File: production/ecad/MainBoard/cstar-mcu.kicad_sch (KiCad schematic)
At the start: 68 parts, among them J25 TYPE-C-31-M-12, J3 RX connect, J31 TYPE-C-31-M-12, J4 TX connect, J5 Ultra_1, J6 Ultra_2, J7 Ultra_3, J8 Ultra_4, Q1 AO3400A, Q2 AO3400A, Q3 AO3400A, Q4 AO3400A, SW1 SW_Push, SW2 SW_Push, SW3 SW_Push, SW4 SW_Push, U1 ESP32-WROOM-32UE_M113EH6400UH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, U10 TCA9534PWR, U2 CP2102N-A01-GQFN28, U3 TXB0104DR, U4 CP2102N-A01-GQFN28, U5 TXB0104DR, U6 ESP32-WROOM-32UE_M113EH6400UH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

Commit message: fixed some sch mistakes, more layout
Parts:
- removed R9 (x2): 4.7k, Resistor_SMD:R_0805_2012Metric, symbol Device:R
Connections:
- net +3.3V is gone; now on net +3V3: R9.2, R9.2, R9.2, R9.2, R9.2, U10.16 (VCC), U3.1 (VCCA), U5.1 (VCCA)

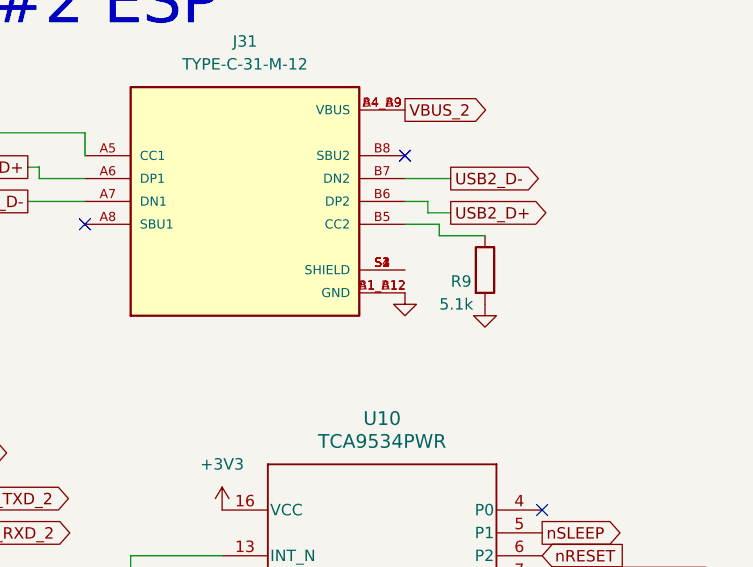
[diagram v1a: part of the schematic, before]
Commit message: ALL DRC ERRORS FIXED
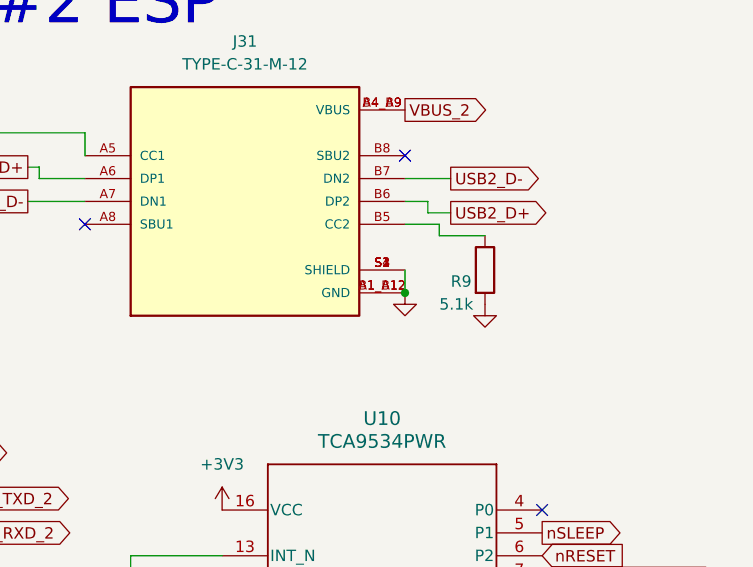
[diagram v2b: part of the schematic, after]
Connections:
- net GND: now also J31.S1 (SHIELD), J31.S2 (SHIELD), J31.S3 (SHIELD), J31.S4 (SHIELD)
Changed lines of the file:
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@@
   (junction (at 36.83 148.59) (diameter 0) (color 0 0 0 0)
+  )
+  (junction (at 377.19 137.16) (diameter 0) (color 0 0 0 0)
   )
   (junction (at 177.165 24.765) (diameter 0) (color 0 0 0 0)
@@
     (stroke (width 0) (type default))
   )
+  (wire (pts (xy 377.19 134.62) (xy 377.19 137.16))
+    (stroke (width 0) (type default))
+  )

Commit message: fixed usbc
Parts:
- removed J25, J31: TYPE-C-31-M-12, CSTAR-MainBoard-Footprints:HRO_TYPE-C-31-M-12, symbol TYPE-C-31-M-12:TYPE-C-31-M-12
- removed R9 (x4): 5.1k, Resistor_SMD:R_0805_2012Metric, symbol Device:R
- added J25, J27: DX07S016JA3R1500, CONN12_DX07S_JAE, symbol usbc:DX07S016JA3R1500
- added R9 (x4): 5.1k, Resistor_SMD:R_0805_2012Metric, symbol Device:R
- added R9 (x2): 4.7k, Resistor_SMD:R_0805_2012Metric, symbol Device:R
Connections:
- net USB1_D- is gone; now on net USB1_D+: U2.5 (D-)
- net USB2_D- is gone; now on net USB2_D+: U4.5 (D-)
- net +3V3: now also R9.1, R9.1; no longer R9.2, R9.2, R9.2, R9.2, R9.2, U10.16 (VCC), U3.1 (VCCA), U5.1 (VCCA)
- net GND: now also J25.1 (GND), J25.12 (GND), J27.1 (GND), J27.12 (GND), R9.2, R9.2, R9.2, R9.2
- net SCL: now also R9.2
- net SDA: now also R9.2
- net USB1_D+: now also J27.5 (D-), J27.6 (D+), J27.7 (D+), J27.8 (D-)
- net USB2_D+: now also J25.5 (D-), J25.6 (D+), J25.7 (D+)
- net VBUS_1: now also J27.11 (VBUS), J27.2 (VBUS)
- net VBUS_2: now also J25.11 (VBUS), J25.2 (VBUS)
- new net: J25.3 (CC1), R9.1
- new net: J27.3 (CC1), R9.1
- new net: J25.9 (CC2), R9.1
- new net: J27.9 (CC2), R9.1
- new net +3.3V: R9.2, R9.2, R9.2, R9.2, R9.2, U10.16 (VCC), U3.1 (VCCA), U5.1 (VCCA)

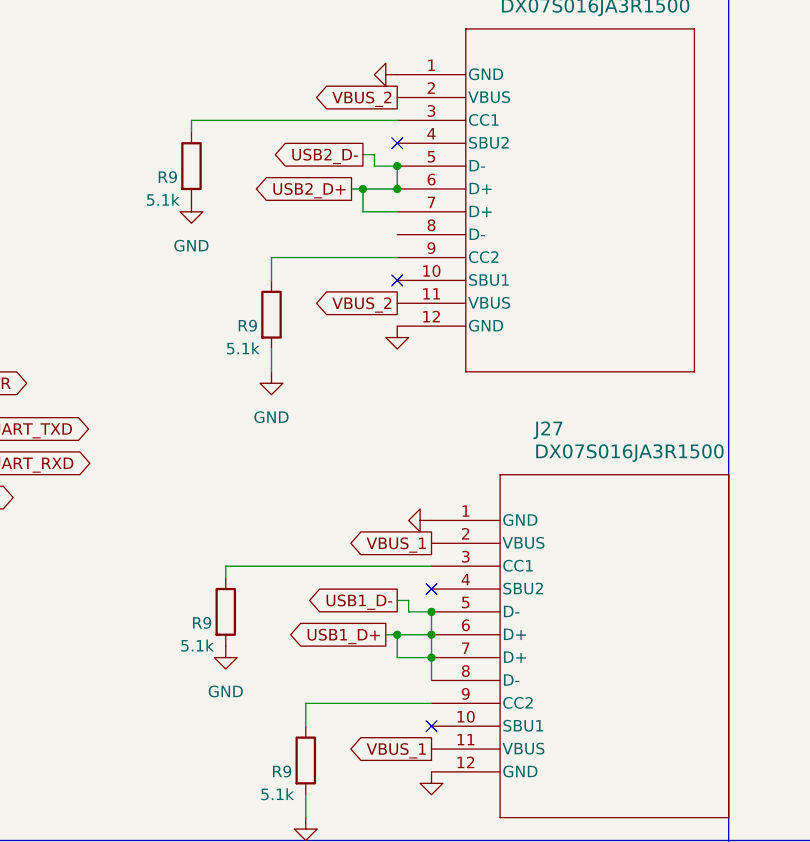
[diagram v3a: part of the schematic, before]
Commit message: fixed cats weird usbc thing (FIX YOUR FOOTPRINT)
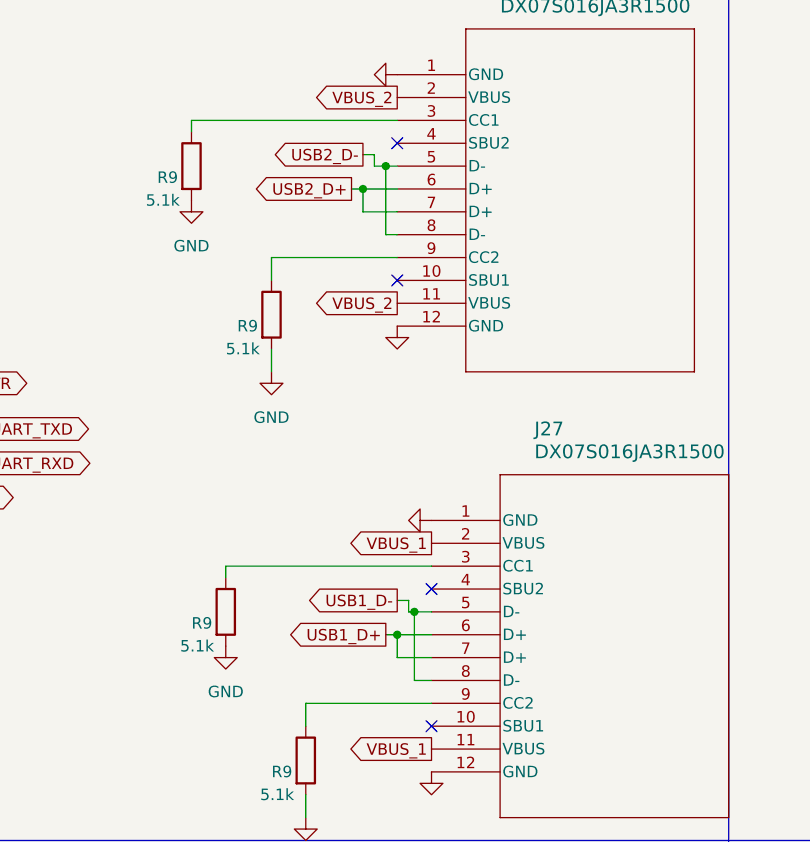
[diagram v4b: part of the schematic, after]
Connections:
- net USB1_D+: no longer J27.5 (D-), J27.8 (D-), U2.5 (D-)
- net USB2_D+: no longer J25.5 (D-), U4.5 (D-)
- net USB2_D-: now reaches J25.8 (D-)
- net USB2_D-: now also J25.5 (D-), U4.5 (D-)
- new net USB1_D-: J27.5 (D-), J27.8 (D-), U2.5 (D-)
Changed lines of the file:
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@@
   (junction (at 383.54 23.495) (diameter 0) (color 0 0 0 0)
   )
+  (junction (at 171.45 128.27) (diameter 0) (color 0 0 0 0)
+  )
   (junction (at 322.58 224.79) (diameter 0) (color 0 0 0 0)
   )
@@
   (junction (at 196.85 34.925) (diameter 0) (color 0 0 0 0)
   )
-  (junction (at 172.72 130.81) (diameter 0) (color 0 0 0 0)
-  )
   (junction (at 168.91 130.81) (diameter 0) (color 0 0 0 0)
   )
@@
   (junction (at 245.11 167.64) (diameter 0) (color 0 0 0 0)
   )
-  (junction (at 176.53 177.8) (diameter 0) (color 0 0 0 0)
-  )
   (junction (at 392.43 222.25) (diameter 0) (color 0 0 0 0)
   )
@@
   (junction (at 398.78 55.88) (diameter 0) (color 0 0 0 0)
   )
-  (junction (at 176.53 182.88) (diameter 0) (color 0 0 0 0)
-  )
   (junction (at 133.35 251.46) (diameter 0) (color 0 0 0 0)
   )
@@
   (junction (at 356.87 186.69) (diameter 0) (color 0 0 0 0)
   )
-  (junction (at 176.53 180.34) (diameter 0) (color 0 0 0 0)
-  )
   (junction (at 387.35 33.655) (diameter 0) (color 0 0 0 0)
   )
   (junction (at 193.675 24.765) (diameter 0) (color 0 0 0 0)
   )
-  (junction (at 172.72 128.27) (diameter 0) (color 0 0 0 0)
+  (junction (at 174.625 177.8) (diameter 0) (color 0 0 0 0)
   )
   (junction (at 36.83 139.7) (diameter 0) (color 0 0 0 0)
@@
     (stroke (width 0) (type default))
   )
+  (wire (pts (xy 172.72 182.88) (xy 176.53 182.88))
+    (stroke (width 0) (type default))
+  )
   (wire (pts (xy 383.54 23.495) (xy 383.54 26.035))
     (stroke (width 0) (type default))
@@
   )
   (wire (pts (xy 248.92 167.64) (xy 245.11 167.64))
+    (stroke (width 0) (type default))
+  )
+  (wire (pts (xy 171.45 128.27) (xy 170.18 128.27))
     (stroke (width 0) (type default))
   )
@@
     (stroke (width 0) (type default))
   )
-  (wire (pts (xy 176.53 177.8) (xy 173.99 177.8))
+  (wire (pts (xy 174.625 177.8) (xy 173.99 177.8))
+    (stroke (width 0) (type default))
+  )
+  (wire (pts (xy 176.53 177.8) (xy 174.625 177.8))
     (stroke (width 0) (type default))
   )
@@
     (stroke (width 0) (type default))
   )
-  (wire (pts (xy 172.72 128.27) (xy 170.18 128.27))
+  (wire (pts (xy 172.72 128.27) (xy 171.45 128.27))
     (stroke (width 0) (type default))
   )
@@
   )
   (wire (pts (xy 346.71 181.61) (xy 346.71 185.42))
+    (stroke (width 0) (type default))
+  )
+  (wire (pts (xy 174.625 177.8) (xy 174.625 185.42))
     (stroke (width 0) (type default))
   )
@@
     (stroke (width 0) (type default))
   )
-  (wire (pts (xy 176.53 182.88) (xy 172.72 182.88))
-    (stroke (width 0) (type default))
-  )
   (wire (pts (xy 369.57 73.66) (xy 369.57 71.12))
     (stroke (width 0) (type default))
@@
     (stroke (width 0) (type default))
   )
-  (wire (pts (xy 176.53 180.34) (xy 176.53 182.88))
-    (stroke (width 0) (type default))
-  )
   (wire (pts (xy 115.57 162.56) (xy 119.38 162.56))
     (stroke (width 0) (type default))
@@
     (stroke (width 0) (type default))
   )
-  (wire (pts (xy 176.53 182.88) (xy 176.53 185.42))
-    (stroke (width 0) (type default))
-  )
   (wire (pts (xy 361.95 60.96) (xy 364.49 60.96))
     (stroke (width 0) (type default))
@@
     (stroke (width 0) (type default))
   )
+  (wire (pts (xy 171.45 128.27) (xy 171.45 135.89))
+    (stroke (width 0) (type default))
+  )
   (wire (pts (xy 361.95 45.72) (xy 368.3 45.72))
     (stroke (width 0) (type default))
@@
     (stroke (width 0) (type default))
   )
-  (wire (pts (xy 176.53 177.8) (xy 176.53 180.34))
-    (stroke (width 0) (type default))
-  )
   (wire (pts (xy 177.165 24.765) (xy 193.675 24.765))
     (stroke (width 0) (type default))
@@
   )
   (wire (pts (xy 401.32 48.26) (xy 398.78 48.26))
+    (stroke (width 0) (type default))
+  )
+  (wire (pts (xy 174.625 185.42) (xy 176.53 185.42))
     (stroke (width 0) (type default))
   )
@@
     (stroke (width 0) (type default))
   )
+  (wire (pts (xy 171.45 135.89) (xy 172.72 135.89))
+    (stroke (width 0) (type default))
+  )
   (wire (pts (xy 118.11 144.78) (xy 115.57 144.78))
     (stroke (width 0) (type default))
@@
     (stroke (width 0) (type default))
   )
-  (wire (pts (xy 172.72 128.27) (xy 172.72 130.81))
-    (stroke (width 0) (type default))
-  )

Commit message: fixed, please for the love of god Kaden dont find any mistakes
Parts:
- removed J25, J27: DX07S016JA3R1500, CONN12_DX07S_JAE, symbol usbc:DX07S016JA3R1500
- removed R9 (x4): 5.1k, Resistor_SMD:R_0805_2012Metric, symbol Device:R
- added J25, J31: USB4105-GF-A, USB4105_GCT, symbol usbfinal:USB4105-GF-A
- added R9 (x4): 5.1k, Resistor_SMD:R_0805_2012Metric, symbol Device:R
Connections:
- net GND: now also J25.A1-B12 (GND), J25.B1-A12 (GND), J31.A1-B12 (GND), J31.B1-A12 (GND), R9.2, R9.2, R9.2, R9.2
- net USB1_D+: now also J25.A6 (DP1), J25.B6 (DP2)
- net USB1_D-: now also J25.A7 (DN1), J25.B7 (DN2)
- net USB2_D+: now also J31.A6 (DP1), J31.B6 (DP2)
- net USB2_D-: now also J31.A7 (DN1), J31.B7 (DN2)
- net VBUS_1: now also J25.A4-B9 (VBUS), J25.B4-A9 (VBUS)
- net VBUS_2: now also J31.A4-B9 (VBUS), J31.B4-A9 (VBUS)
- new net: J25.B5 (CC2), R9.1
- new net: J31.A5 (CC1), R9.1
- new net: J31.B5 (CC2), R9.1
- new net: J25.A5 (CC1), R9.1

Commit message: i swear to god kaden this should work
I checked the footprint twice in foortprint editor and everything looks good. I checked to make sure its assigned
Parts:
- removed J25, J31: USB4105-GF-A, USB4105_GCT, symbol usbfinal:USB4105-GF-A
- removed R9 (x4): 5.1k, Resistor_SMD:R_0805_2012Metric, symbol Device:R
- added J27, J31: 1332645, 1332645:PHOENIX_1332645, symbol 1332645:1332645
- added R9 (x4): 5.1k, Resistor_SMD:R_0805_2012Metric, symbol Device:R
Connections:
- net GND: now also J27.A1_B12 (GND_A), J27.B1_A12 (GND_B), J27.SH1 (SHIELD), J27.SH2 (SHIELD__1), J27.SH3 (SHIELD__2), J27.SH4 (SHIELD__3), J31.A1_B12 (GND_A), J31.B1_A12 (GND_B), J31.SH1 (SHIELD), J31.SH2 (SHIELD__1), J31.SH3 (SHIELD__2), J31.SH4 (SHIELD__3), R9.2, R9.2, R9.2, R9.2
- net USB1_D+: now also J31.A6 (DP1), J31.B6 (DP2)
- net USB1_D-: now also J31.A7 (DN1), J31.B7 (DN2)
- net USB2_D+: now also J27.A6 (DP1), J27.B6 (DP2)
- net USB2_D-: now also J27.A7 (DN1), J27.B7 (DN2)
- net VBUS_1: now also J31.A4_B9 (VBUS_A), J31.B4_A9 (VBUS_B)
- net VBUS_2: now also J27.A4_B9 (VBUS_A), J27.B4_A9 (VBUS_B)
- new net: J31.A5 (CC1), R9.1
- new net: J27.B5 (CC2), R9.1
- new net: J31.B5 (CC2), R9.1
- new net: J27.A5 (CC1), R9.1

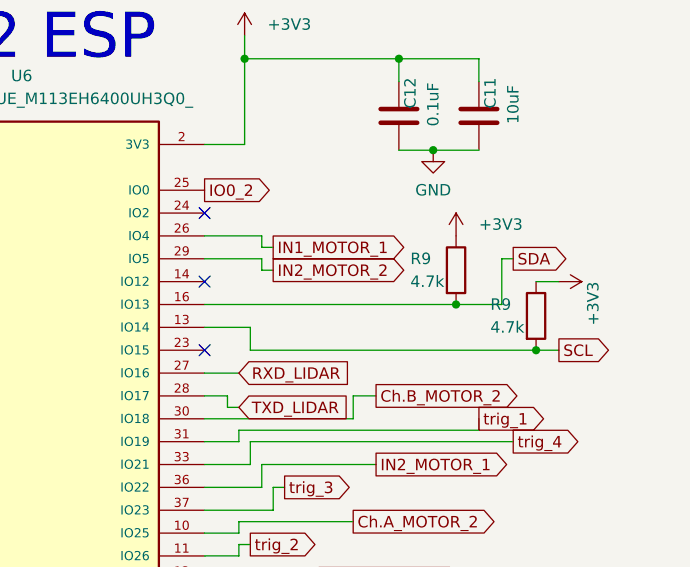
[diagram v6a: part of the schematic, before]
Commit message: updated with correct USBC -- still need to fix added DRCs
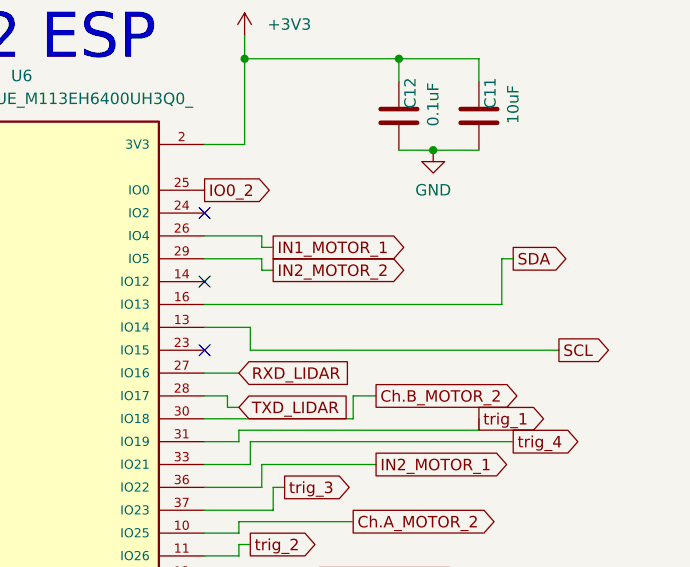
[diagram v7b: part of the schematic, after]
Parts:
- removed R9 (x2): 4.7k, Resistor_SMD:R_0805_2012Metric, symbol Device:R
- J27, J31: footprint 1332645:PHOENIX_1332645 -> CSTAR-MainBoard-Footprints:PHOENIX_1332645
- U10: footprint PW0016A-IPC_A -> CSTAR-MainBoard-Footprints:PW0016A-IPC_A
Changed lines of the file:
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@@
   (junction (at 392.43 222.25) (diameter 0) (color 0 0 0 0)
   )
-  (junction (at 389.89 50.8) (diameter 0) (color 0 0 0 0)
-  )
   (junction (at 236.22 151.13) (diameter 0) (color 0 0 0 0)
   )
@@
   (junction (at 45.72 165.1) (diameter 0) (color 0 0 0 0)
   )
-  (junction (at 398.78 55.88) (diameter 0) (color 0 0 0 0)
-  )
   (junction (at 157.48 138.43) (diameter 0) (color 0 0 0 0)
   )
@@
     (stroke (width 0) (type default))
   )
-  (wire (pts (xy 389.89 50.8) (xy 394.97 50.8))
+  (wire (pts (xy 361.95 50.8) (xy 394.97 50.8))
     (stroke (width 0) (type default))
   )
@@
     (stroke (width 0) (type default))
   )
-  (wire (pts (xy 389.89 50.8) (xy 361.95 50.8))
-    (stroke (width 0) (type default))
-  )
   (wire (pts (xy 264.16 231.14) (xy 264.16 224.79))
     (stroke (width 0) (type default))
@@
     (stroke (width 0) (type default))
   )
-  (wire (pts (xy 401.32 48.26) (xy 398.78 48.26))
-    (stroke (width 0) (type default))
-  )
   (wire (pts (xy 48.26 153.67) (xy 48.26 154.94))
     (stroke (width 0) (type default))
@@
     (stroke (width 0) (type default))
   )
-  (wire (pts (xy 398.78 55.88) (xy 401.32 55.88))
+  (wire (pts (xy 367.03 55.88) (xy 401.32 55.88))
     (stroke (width 0) (type default))
   )
@@
     (stroke (width 0) (type default))
   )
-  (wire (pts (xy 367.03 55.88) (xy 398.78 55.88))
-    (stroke (width 0) (type default))
-  )
   (wire (pts (xy 228.6 171.45) (xy 228.6 167.64))
     (stroke (width 0) (type default))
@@
       (effects (font (size 1.524 1.524)))
     )
-    (property "Footprint" "PW0016A-IPC_A" (at 356.87 161.29 0)
+    (property "Footprint" "CSTAR-MainBoard-Footprints:PW0016A-IPC_A" (at 356.87 161.29 0)
       (effects (font (size 1.27 1.27) italic) hide)
     )
@@
     )
   )
-  (symbol (lib_id "Device:R") (at 398.78 52.07 0) (unit 1)
-    (in_bom yes) (on_board yes) (dnp no)
-    (property "Reference" "R9" (at 393.7 50.8 0)
-      (effects (font (size 1.27 1.27)) (justify left))
-    )
-    (property "Value" "4.7k" (at 393.7 53.34 0)
-      (effects (font (size 1.27 1.27)) (justify left))
-    )
-    (property "Footprint" "Resistor_SMD:R_0805_2012Metric" (at 397.002 52.07 90)
-      (effects (font (size 1.27 1.27)) hide)
-    )
-    (property "Datasheet" "~" (at 398.78 52.07 0)
-      (effects (font (size 1.27 1.27)) hide)
-    )
-    (pin "1")
-    (pin "2")
-    (instances
-      (project "cstar-mcu"
-        (path "/889d461f-2713-421f-88e2-0d0ce2e66089"
-          (reference "R9") (unit 1)
-        )
-      )
-      (project "CSTAR"
-        (path "/cd9fa943-c6eb-468b-990c-ea873c442553/ab376fb8-b3cc-4961-835f-6ea621157706"
-          (reference "R56") (unit 1)
-        )
-      )
-    )
-  )
   (symbol (lib_id "power:GND") (at 22.86 25.4 270) (unit 1)
     (in_bom yes) (on_board yes) (dnp no) (fields_autoplaced)
@@
     )
   )
-  (symbol (lib_id "power:+3V3") (at 389.89 43.18 0) (unit 1)
-    (in_bom yes) (on_board yes) (dnp no)
-    (property "Reference" "#PWR057" (at 389.89 46.99 0)
-      (effects (font (size 1.27 1.27)) hide)
-    )
-    (property "Value" "+3V3" (at 392.43 41.91 0)
-      (effects (font (size 1.27 1.27)) (justify left))
-    )
-    (property "Footprint" "" (at 389.89 43.18 0)
-      (effects (font (size 1.27 1.27)) hide)
-    )
-    (property "Datasheet" "" (at 389.89 43.18 0)
-      (effects (font (size 1.27 1.27)) hide)
-    )
-    (pin "1")
-    (instances
-      (project "cstar-mcu"
-        (path "/889d461f-2713-421f-88e2-0d0ce2e66089"
-          (reference "#PWR057") (unit 1)
-        )
-      )
-      (project "CSTAR"
-        (path "/cd9fa943-c6eb-468b-990c-ea873c442553/ab376fb8-b3cc-4961-835f-6ea621157706"
-          (reference "#PWR0141") (unit 1)
-        )
-      )
-    )
-  )
   (symbol (lib_id "ESP32-WROOM-32UE_M113EH6400UH3Q0_:ESP32-WROOM-32UE_M113EH6400UH3Q0_") (at 153.67 60.96 0) (unit 1)
     (in_bom yes) (on_board yes) (dnp no) (fields_autoplaced)
@@
     )
   )
-  (symbol (lib_id "Device:R") (at 389.89 46.99 0) (unit 1)
-    (in_bom yes) (on_board yes) (dnp no)
-    (property "Reference" "R9" (at 384.81 45.72 0)
-      (effects (font (size 1.27 1.27)) (justify left))
-    )
-    (property "Value" "4.7k" (at 384.81 48.26 0)
-      (effects (font (size 1.27 1.27)) (justify left))
-    )
-    (property "Footprint" "Resistor_SMD:R_0805_2012Metric" (at 388.112 46.99 90)
-      (effects (font (size 1.27 1.27)) hide)
-    )
-    (property "Datasheet" "~" (at 389.89 46.99 0)
-      (effects (font (size 1.27 1.27)) hide)
-    )
-    (pin "1")
-    (pin "2")
-    (instances
-      (project "cstar-mcu"
-        (path "/889d461f-2713-421f-88e2-0d0ce2e66089"
-          (reference "R9") (unit 1)
-        )
-      )
-      (project "CSTAR"
-        (path "/cd9fa943-c6eb-468b-990c-ea873c442553/ab376fb8-b3cc-4961-835f-6ea621157706"
-          (reference "R55") (unit 1)
-        )
-      )
-    )
-  )
   (symbol (lib_id "power:GND") (at 151.13 269.24 0) (unit 1)
     (in_bom yes) (on_board yes) (dnp no) (fields_autoplaced)
@@
       (effects (font (size 1.27 1.27)))
     )
-    (property "Footprint" "1332645:PHOENIX_1332645" (at 175.26 120.65 0)
+    (property "Footprint" "CSTAR-MainBoard-Footprints:PHOENIX_1332645" (at 175.26 120.65 0)
       (effects (font (size 1.27 1.27)) (justify bottom) hide)
     )
@@
       (effects (font (size 1.27 1.27)))
     )
-    (property "Footprint" "1332645:PHOENIX_1332645" (at 173.99 161.29 0)
+    (property "Footprint" "CSTAR-MainBoard-Footprints:PHOENIX_1332645" (at 173.99 161.29 0)
       (effects (font (size 1.27 1.27)) (justify bottom) hide)
     )
@@
         )
       )
-    )
-  )
-  (symbol (lib_id "power:+3V3") (at 401.32 48.26 270) (unit 1)
-    (in_bom yes) (on_board yes) (dnp no)
-    (property "Reference" "#PWR057" (at 397.51 48.26 0)
-      (effects (font (size 1.27 1.27)) hide)
-    )
-    (property "Value" "+3V3" (at 405.13 48.26 0)
-      (effects (font (size 1.27 1.27)) (justify left))
-    )
-    (property "Footprint" "" (at 401.32 48.26 0)
-      (effects (font (size 1.27 1.27)) hide)
-    )
-    (property "Datasheet" "" (at 401.32 48.26 0)
-      (effects (font (size 1.27 1.27)) hide)
-    )
-    (pin "1")
-    (instances
-      (project "cstar-mcu"
-        (path "/889d461f-2713-421f-88e2-0d0ce2e66089"
-          (reference "#PWR057") (unit 1)
-        )
-      )
-      (project "CSTAR"
-        (path "/cd9fa943-c6eb-468b-990c-ea873c442553/ab376fb8-b3cc-4961-835f-6ea621157706"
-          (reference "#PWR0142") (unit 1)
-        )
-      )

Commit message: final touches on PCB
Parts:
- added J25: Conn_01x06_Socket, symbol Connector:Conn_01x06_Socket
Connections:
- net +3.3V is gone; now on net +3V3: R9.2, R9.2, R9.2, R9.2, R9.2, U10.16 (VCC), U3.1 (VCCA), U5.1 (VCCA)
- net at U1.10 (IO25): now also J25.4 (Pin_4)
- net at U1.12 (IO27): now also J25.5 (Pin_5)
- net at U1.14 (IO12): now also J25.6 (Pin_6)
- net pin_4: now reaches U1.6 (IO34)
- net pin_4: now also J25.1 (Pin_1)
- net pin_5: now reaches U1.7 (IO35)
- net pin_5: now also J25.2 (Pin_2)
- net at U1.8 (IO32): now also J25.3 (Pin_3)
- no-connect marks 59 -> 53
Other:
- moved on the sheet: C10, C9, U1
